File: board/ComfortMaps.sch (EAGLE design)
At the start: 46 parts, among them J1 PROG_HDR, J5 0545482271, J6 0545482271, U1 ADXL362, U3 ADP160-3.3, U4 MCP73833, X1 RASPI_GPIO_B+#_PIN

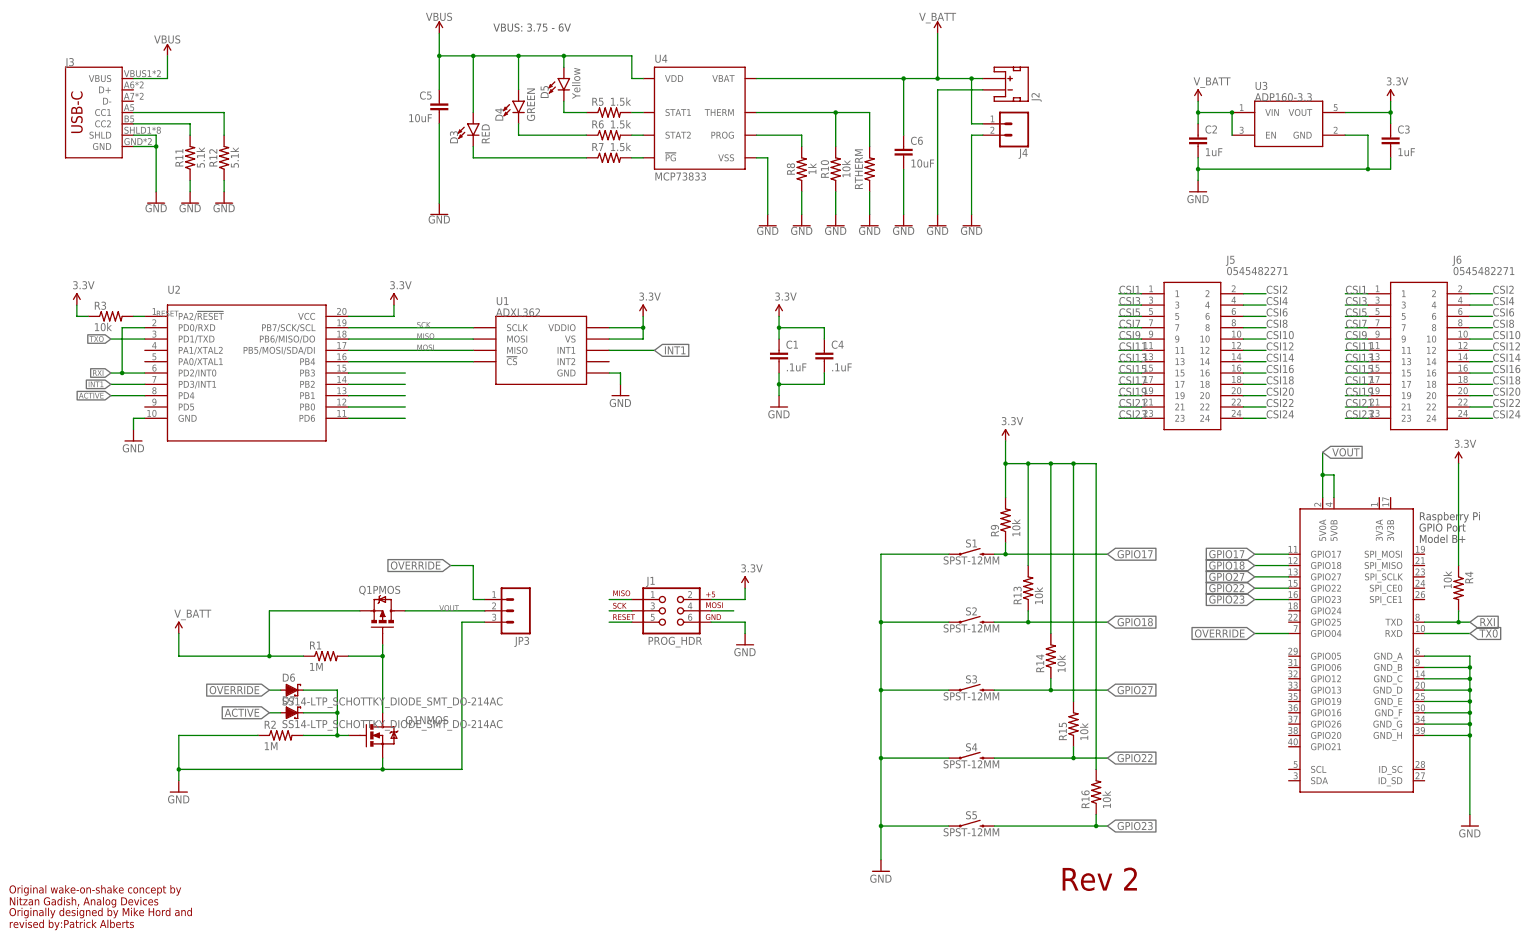
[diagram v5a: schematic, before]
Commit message: v3 of the board, with new mounting holes and an added LED for V_out.
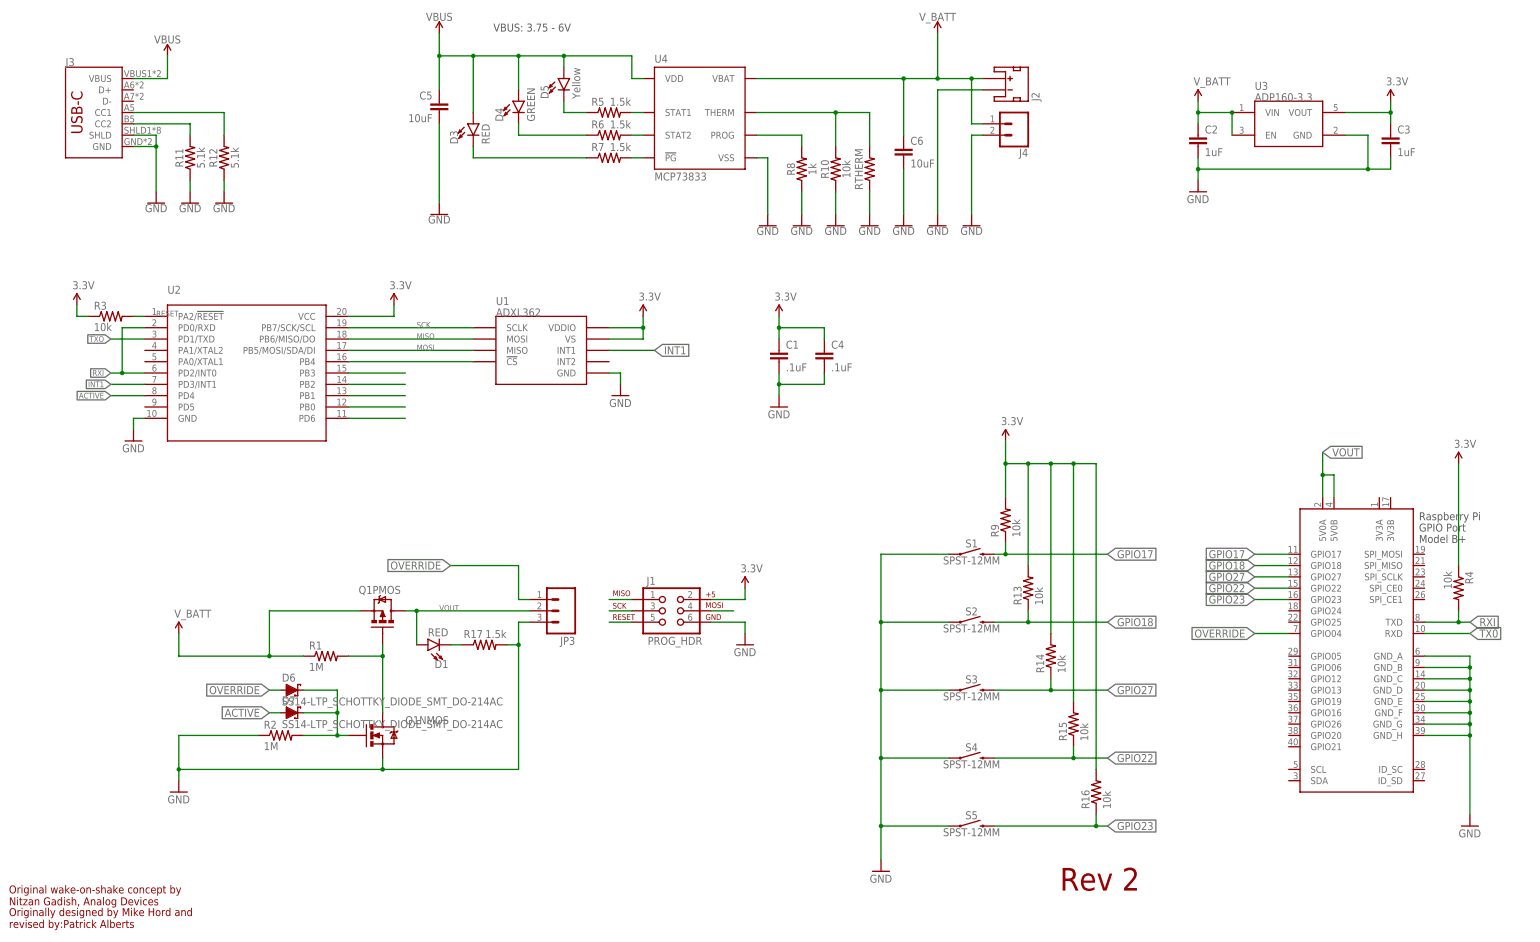
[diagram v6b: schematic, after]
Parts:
- removed J5, J6: 0545482271, 0545482271:0545482271
- added D1: RED, SparkFun-LED:LED-RED0603
- added R17: 1.5k, SparkFun-Resistors:1.5KOHM-0603-1/10W-1%
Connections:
- removed net CSI1: J5.1, J6.1
- removed net CSI10: J5.10, J6.10
- removed net CSI11: J5.11, J6.11
- removed net CSI12: J5.12, J6.12
- removed net CSI13: J5.13, J6.13
- removed net CSI14: J5.14, J6.14
- removed net CSI15: J5.15, J6.15
- removed net CSI16: J5.16, J6.16
- removed net CSI17: J5.17, J6.17
- removed net CSI18: J5.18, J6.18
- removed net CSI19: J5.19, J6.19
- removed net CSI2: J5.2, J6.2
- removed net CSI20: J5.20, J6.20
- removed net CSI21: J5.21, J6.21
- removed net CSI22: J5.22, J6.22
- removed net CSI23: J5.23, J6.23
- removed net CSI24: J5.24, J6.24
- removed net CSI3: J5.3, J6.3
- removed net CSI4: J5.4, J6.4
- removed net CSI5: J5.5, J6.5
- removed net CSI6: J5.6, J6.6
- removed net CSI7: J5.7, J6.7
- removed net CSI8: J5.8, J6.8
- removed net CSI9: J5.9, J6.9
- new net N$14: D1.C, R17.1
- net GND: now also R17.2
- net VOUT: now also D1.A
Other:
- moved on the sheet: JP3

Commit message: Enlarging spst button pads and connecting both sides.
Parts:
- S1, S2, S3, S4, S5: device SparkFun-Switches:MOMENTARY-SWITCH-SPST-SMD-12MM -> CM-SparkFun-Switches:MOMENTARY-SWITCH-SPST-SMD-12MM
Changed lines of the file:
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@@
 </part>
 <part name="P+7" library="SparkFun-Aesthetics" deviceset="3.3V" device=""/>
-<part name="S1" library="SparkFun-Switches" library_urn="urn:adsk.eagle:library:535" deviceset="MOMENTARY-SWITCH-SPST" device="-SMD-12MM" package3d_urn="urn:adsk.eagle:package:40166/1" value="SPST-12MM"/>
-<part name="S2" library="SparkFun-Switches" library_urn="urn:adsk.eagle:library:535" deviceset="MOMENTARY-SWITCH-SPST" device="-SMD-12MM" package3d_urn="urn:adsk.eagle:package:40166/1" override_package3d_urn="urn:adsk.eagle:package:15371983/2" override_package_urn="urn:adsk.eagle:footprint:40109/1" value="SPST-12MM"/>
-<part name="S3" library="SparkFun-Switches" library_urn="urn:adsk.eagle:library:535" deviceset="MOMENTARY-SWITCH-SPST" device="-SMD-12MM" package3d_urn="urn:adsk.eagle:package:40166/1" value="SPST-12MM"/>
-<part name="S4" library="SparkFun-Switches" library_urn="urn:adsk.eagle:library:535" deviceset="MOMENTARY-SWITCH-SPST" device="-SMD-12MM" package3d_urn="urn:adsk.eagle:package:40166/1" value="SPST-12MM"/>
-<part name="S5" library="SparkFun-Switches" library_urn="urn:adsk.eagle:library:535" deviceset="MOMENTARY-SWITCH-SPST" device="-SMD-12MM" package3d_urn="urn:adsk.eagle:package:40166/1" value="SPST-12MM"/>
+<part name="S1" library="CM-SparkFun-Switches" deviceset="MOMENTARY-SWITCH-SPST" device="-SMD-12MM" value="SPST-12MM"/>
+<part name="S2" library="CM-SparkFun-Switches" deviceset="MOMENTARY-SWITCH-SPST" device="-SMD-12MM" override_package3d_urn="urn:adsk.eagle:package:15371983/2" override_package_urn="urn:adsk.eagle:footprint:40109/1" override_locally_modified="yes" value="SPST-12MM"/>
+<part name="S3" library="CM-SparkFun-Switches" deviceset="MOMENTARY-SWITCH-SPST" device="-SMD-12MM" value="SPST-12MM"/>
+<part name="S4" library="CM-SparkFun-Switches" deviceset="MOMENTARY-SWITCH-SPST" device="-SMD-12MM" value="SPST-12MM"/>
+<part name="S5" library="CM-SparkFun-Switches" deviceset="MOMENTARY-SWITCH-SPST" device="-SMD-12MM" value="SPST-12MM"/>
 <part name="P+8" library="SparkFun-Aesthetics" deviceset="3.3V" device=""/>
 <part name="X1" library="raspberrypi_bastelstube_v13" deviceset="RASPI_GPIO_B+#" device="_PIN"/>
